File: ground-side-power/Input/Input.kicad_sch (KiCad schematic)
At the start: 36 parts, among them J1 Battery Terminals, J2 Battery Terminals, J26 Conn_01x02_Female, J3 Battery Terminals, J4 Battery Terminals, J5 874270842, J6 874270842, J7 ATX-24, J8 Conn_01x03_Female, J9 Conn_01x03_Female, K1 AZ2150-1A-12DEF, M1 Fan_PC_Chassis, SW1 GRB234A2NABA1, U1 INA180, U2 INA180

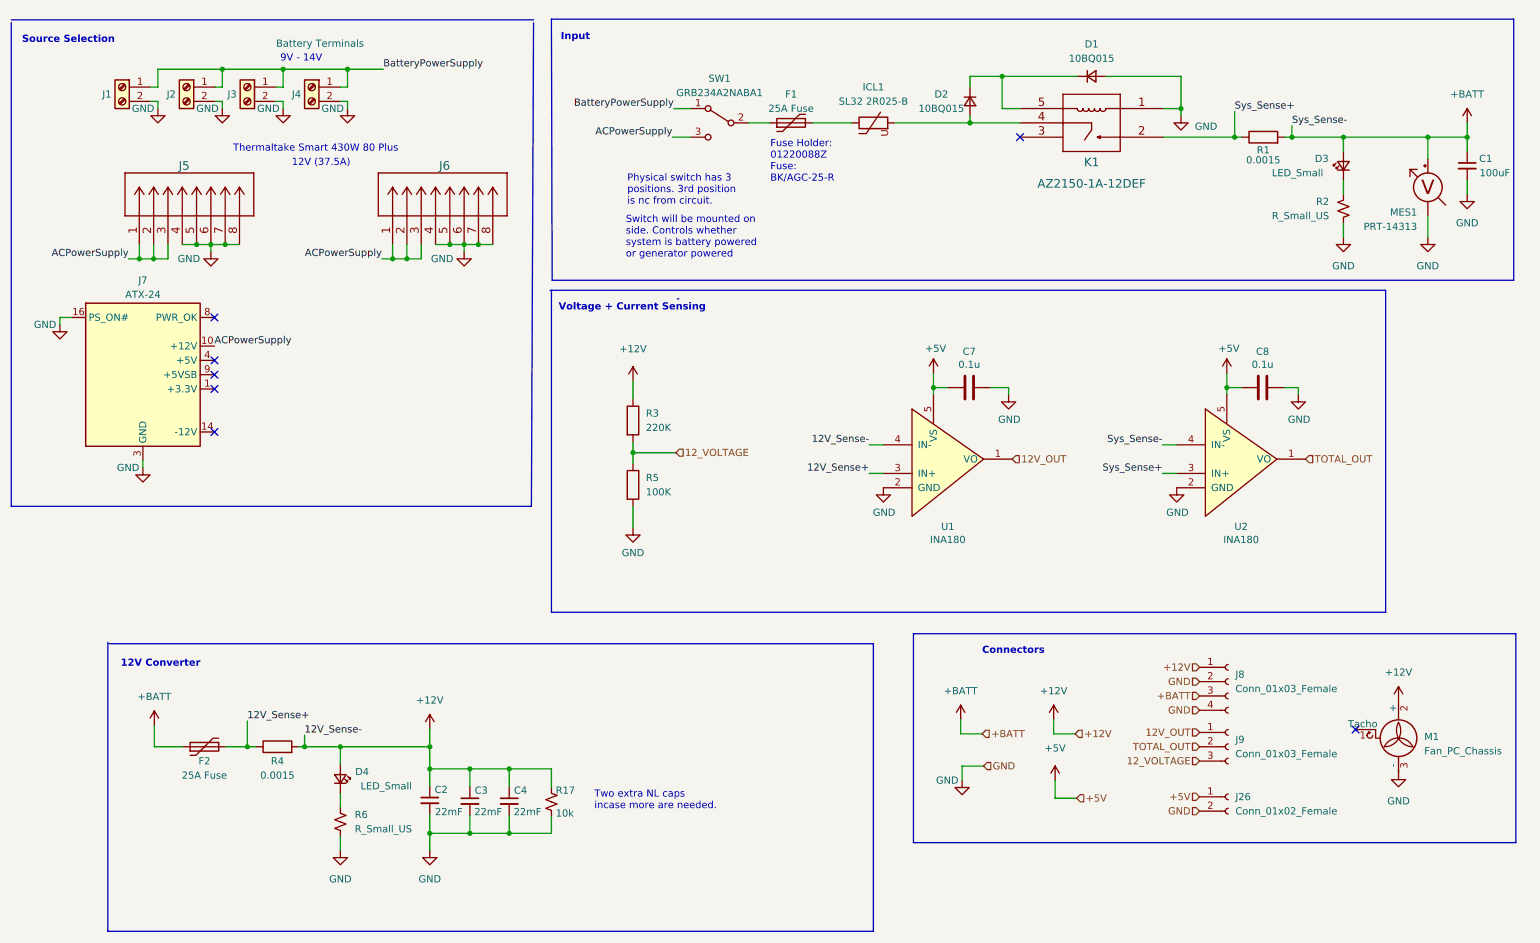
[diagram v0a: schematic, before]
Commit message: Fixed footprint issue
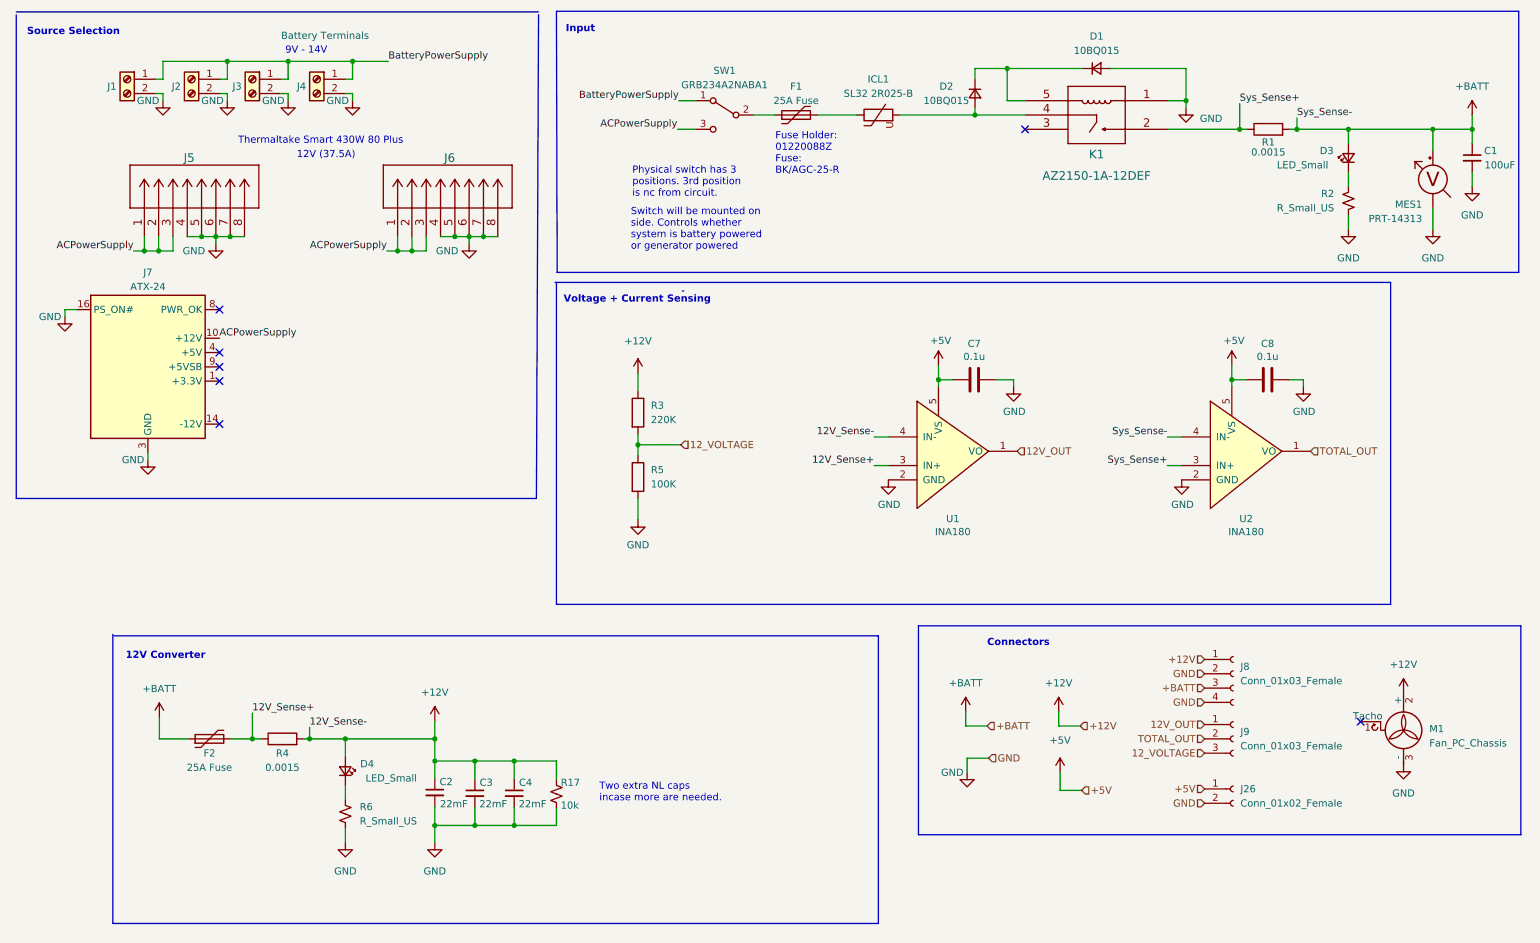
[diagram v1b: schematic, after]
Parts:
- MES1: footprint GSP:OSTTA020161 -> GSP:1935310
